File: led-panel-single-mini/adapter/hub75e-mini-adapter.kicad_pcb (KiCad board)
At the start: 2 copper layers, 10.1 x 42 mm, 2 parts, among them J1 Conn_02x08_Odd_Even, J2 Conn_02x08_Odd_Even

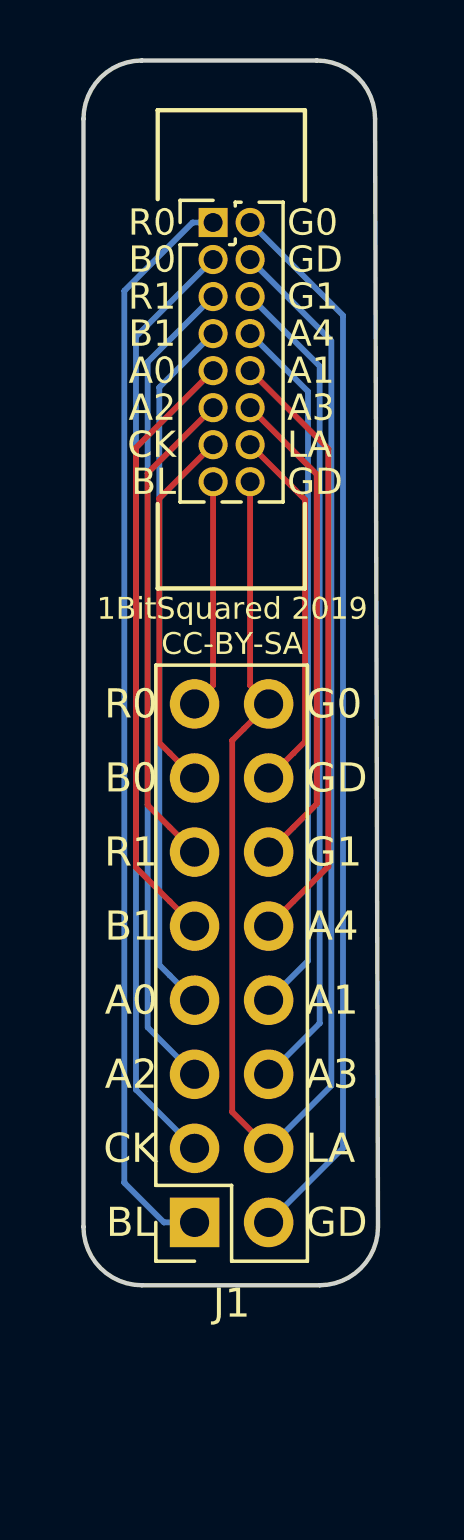
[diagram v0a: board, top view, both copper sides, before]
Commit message: Corrected spacing and legend of the small led panel connector adapter.
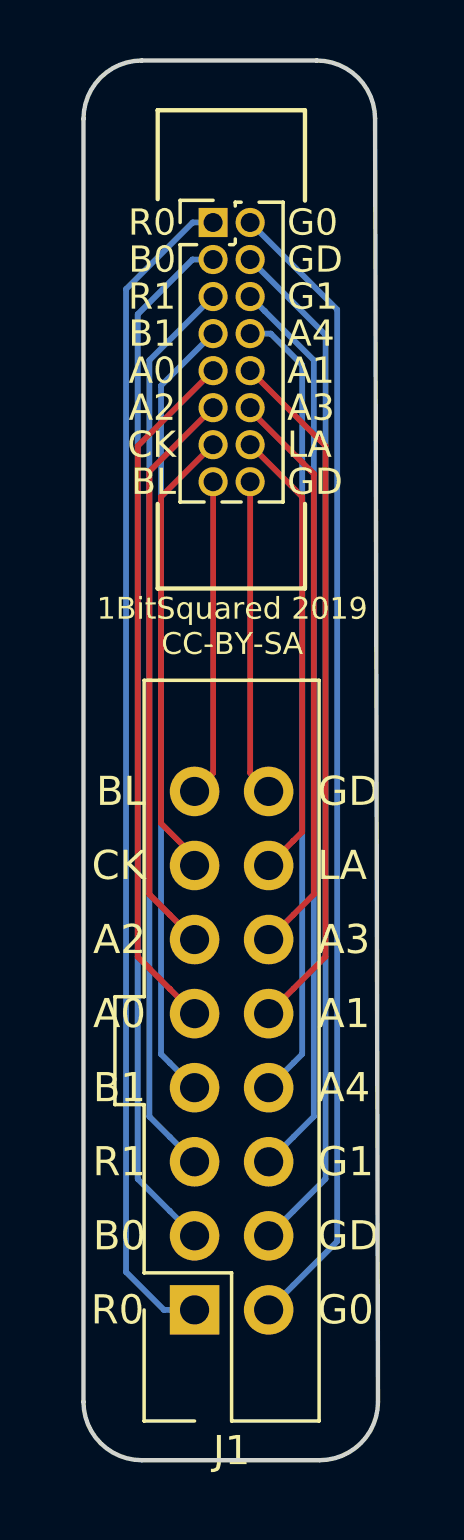
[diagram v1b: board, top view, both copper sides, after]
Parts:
- moved J1 3.00 mm to (41.2, 76.8)
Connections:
- net /A0x renamed /A0
- net /A1x renamed /A1
- net /A2x renamed /A2
- net /A3x renamed /A3
- net /A4x renamed /A4
- net /B1x renamed /B1
- net /BLANKx renamed /BLANK
- net /Bx renamed /B0
- net /G1x renamed /G1
- net /Gx renamed /G0
- net /LATCHx renamed /LATCH
- net /R1x renamed /R1
- net /Rx renamed /R0
- net /SCLKx renamed /SCLK
- J1 pad 16: GND -> /GND1
- J1 pad 4: GND -> /GND0
- J2 pad 16: GND -> /GND1
- J2 pad 4: GND -> /GND0
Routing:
- net GND: track 56.7 -> 0.00 mm
- net /GND0: track 0.00 -> 35.4 mm
- net /GND1: track 0.00 -> 10.9 mm
- net /B0: track 32.4 -> 35.8 mm
- net /A4: track 24.2 -> 27.5 mm
- net /BLANK: track 7.88 -> 10.9 mm
- net /R0: track 37.6 -> 40.5 mm
- net /R1: track 28.3 -> 31.2 mm
- net /B1: track 24.1 -> 27.1 mm
- net /SCLK: track 12.7 -> 15.6 mm
- net /A2: track 16.8 -> 19.8 mm
- net /A0: track 21.0 -> 23.9 mm
- net /LATCH: track 12.7 -> 15.6 mm
- net /A3: track 16.9 -> 19.8 mm
- net /A1: track 21.0 -> 23.9 mm
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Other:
- board size 10.1 x 42 mm -> 10.1 x 48 mm

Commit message: Some global cleanup.
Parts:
- added REF**: 1b2_Logo_SilkS_5mm, pkl_logos:1b2_Logo_SilkS_5mm, B.Cu at (42.1, 54.5)
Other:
- board text added: "1Bitsquared"
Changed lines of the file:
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@@
   (general
     (thickness 0.8)
-    (drawings 77)
+    (drawings 78)
     (tracks 66)
     (zones 0)
-    (modules 2)
+    (modules 3)
     (nets 17)
   )
@@
     (add_net /R1)
     (add_net /SCLK)
+  )
+  (module pkl_logos:1b2_Logo_SilkS_5mm locked (layer B.Cu)
+    (at 42.109884 54.5)
+    (fp_text reference REF** (at 0 -4) (layer B.Fab) hide
+      (effects (font (size 1 1) (thickness 0.15)) (justify mirror))
+    )
+    (fp_text value 1b2_Logo_SilkS_5mm (at 0 4) (layer B.Fab) hide
+      (effects (font (size 1 1) (thickness 0.15)) (justify mirror))
+    )
+    (fp_line (start -0.5 0.5) (end -0.5 2.5) (layer B.SilkS) (width 0.2))
+    (fp_line (start -0.5 2.5) (end -2.5 2.5) (layer B.SilkS) (width 0.2))
+    (fp_line (start -2.5 2.5) (end -2.5 0.5) (layer B.SilkS) (width 0.2))
+    (fp_line (start -2.5 0.5) (end -0.5 0.5) (layer B.SilkS) (width 0.2))
+    (fp_line (start -0.5 2.5) (end 0 2) (layer B.SilkS) (width 0.2))
+    (fp_line (start 0 2) (end 0 0) (layer B.SilkS) (width 0.2))
+    (fp_line (start 0 0) (end -0.5 0.5) (layer B.SilkS) (width 0.2))
+    (fp_line (start -2.5 0.5) (end -2 0) (layer B.SilkS) (width 0.2))
+    (fp_line (start -2 0) (end 0 0) (layer B.SilkS) (width 0.2))
+    (fp_line (start 2 2) (end 0.5 2) (layer B.SilkS) (width 0.2))
+    (fp_line (start 0.5 2) (end 0.5 -0.5) (layer B.SilkS) (width 0.2))
+    (fp_line (start 0.5 -0.5) (end -2 -0.5) (layer B.SilkS) (width 0.2))
+    (fp_line (start -2 -0.5) (end -2 -2) (layer B.SilkS) (width 0.2))
+    (fp_line (start -2 -2) (end 2 -2) (layer B.SilkS) (width 0.2))
+    (fp_line (start 2 -2) (end 2 2) (layer B.SilkS) (width 0.2))
+    (fp_line (start 2 2) (end 2.5 1.5) (layer B.SilkS) (width 0.2))
+    (fp_line (start 2.5 1.5) (end 2.5 -2.5) (layer B.SilkS) (width 0.2))
+    (fp_line (start 2.5 -2.5) (end 2 -2) (layer B.SilkS) (width 0.2))
+    (fp_line (start -2 -2) (end -1.5 -2.5) (layer B.SilkS) (width 0.2))
+    (fp_line (start -1.5 -2.5) (end 2.5 -2.5) (layer B.SilkS) (width 0.2))
   )
   (module Connector_PinSocket_2.54mm:PinSocket_2x08_P2.54mm_Vertical (layer F.Cu)
@@
     )
   )
+  (gr_text 1Bitsquared (at 42.309885 50.814174 180) (layer B.SilkS)
+    (effects (font (size 0.75 0.75) (thickness 0.1875)) (justify mirror))
+  )
   (gr_text "HUB75E Mini\nAdapter" (at 42.4 36.3 180) (layer B.SilkS)
